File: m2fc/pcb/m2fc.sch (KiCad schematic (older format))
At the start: 70 parts, among them IC101 ADP3335, IC102 STM32F405VGT, IC103 ADP3335, P101 CONN_2, P102 CONN_2, P103 CONN_2, P104 SWD, U101 BAT BOX, U102 ARM SW, U103 HOUSING, U104 HOUSING, U105 HOUSING, U106 MICROSD, U107 MOUNT, U108 MOUNT, U109 MOUNT, U110 MOUNT, U111 MOUNT, U112 MOUNT, X101 8M

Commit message: routing continues
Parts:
- removed GS103: GS2, Connect:GS2, symbol GS2
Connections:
- net GYRO_INT1: now also IC102.44 (PE13); no longer IC102.46 (PE15)
- net HG_ACCEL_INT1: now also IC102.34 (PC5); no longer IC102.33 (PC4)
- net HG_ACCEL_INT2: now also IC102.33 (PC4); no longer IC102.34 (PC5)
- net SJ3: no longer names the net of IC102.62 (PD15)
- no-connect marks 24 -> 25
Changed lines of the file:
@@
 Text Label 4450 3600 0    60   ~ 0
 SD_CD
+Text Label 4450 2300 0    60   ~ 0
+HG_ACCEL_INT1
 Text Label 4450 2200 0    60   ~ 0
-HG_ACCEL_INT1
-Text Label 4450 2300 0    60   ~ 0
 HG_ACCEL_INT2
 Text Label 4450 4300 0    60   ~ 0
@@
 Text Label 8300 3700 0    60   ~ 0
 GYRO_INT1
-Text Label 4450 6700 0    60   ~ 0
+Text Label 4450 6500 0    60   ~ 0
 GYRO_INT1
 Text Label 6600 5950 2    60   ~ 0
@@
 NoConn ~ 4400 4500
 NoConn ~ 4400 4600
-NoConn ~ 4400 6500
 NoConn ~ 3100 6100
 NoConn ~ 3100 6200
@@
 	0    1    1    0
 $EndComp
-$Comp
-L GS2 GS103
-U 1 1 53CB171F
-P 10550 1150
-F 0 "GS103" H 10650 1300 50  0000 C CNN
-F 1 "GS2" H 10650 1001 40  0000 C CNN
-F 2 "Connect:GS2" V 10624 1150 30  0001 C CNN
-F 3 "" H 10550 1150 60  0000 C CNN
-	1    10550 1150
-	0    1    1    0
-$EndComp
 Text Notes 9900 1500 0    60   ~ 0
 CONFIG JUMPERS
@@
 Text Label 10250 900  2    60   ~ 0
 SJ2
-Text Label 10250 1150 2    60   ~ 0
-SJ3
 Text Label 4450 4800 0    60   ~ 0
 SJ1
 Text Label 4450 4900 0    60   ~ 0
 SJ2
-Text Label 4450 5000 0    60   ~ 0
-SJ3
 $Comp
 L STM32F405VGT IC102
@@
 	3100 5300 3050 5300
 Wire Wire Line
-	4400 6700 4450 6700
-Wire Wire Line
 	4400 6600 4450 6600
+Wire Wire Line
+	4400 6500 4450 6500
 Wire Wire Line
 	4400 4400 4450 4400
@@
 	8250 5400 8300 5400
 Wire Wire Line
-	10750 1150 10800 1150
-Wire Wire Line
 	10800 650  10800 1200
 Wire Wire Line
 	10750 900  10800 900
-Connection ~ 10800 1150
 Wire Wire Line
 	10750 650  10800 650
 Connection ~ 10800 900
 Wire Wire Line
-	10350 1150 10250 1150
-Wire Wire Line
 	10350 900  10250 900
 Wire Wire Line
@@
 Wire Wire Line
 	4400 4900 4450 4900
-Wire Wire Line
-	4400 5000 4450 5000
 Wire Wire Line
 	6050 1900 6050 2350
@@
 NoConn ~ 4400 5700
 NoConn ~ 4400 5800
+NoConn ~ 4400 6700
+NoConn ~ 4400 5000
 $EndSCHEMATC

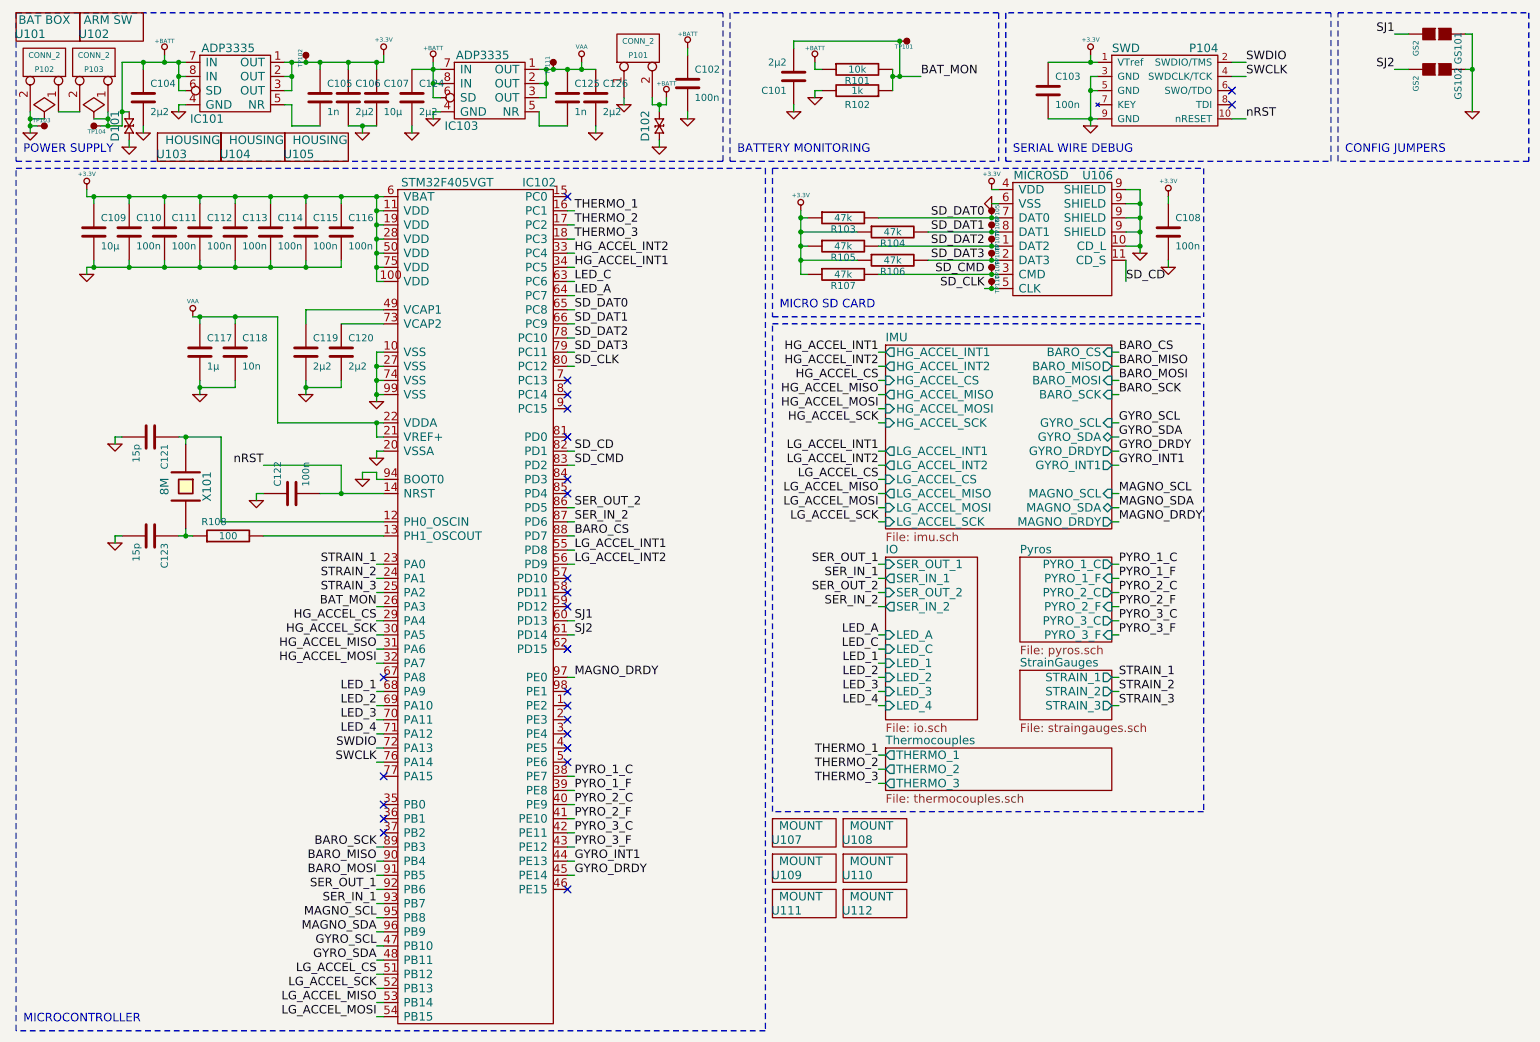
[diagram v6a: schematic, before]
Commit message: routing intensifies
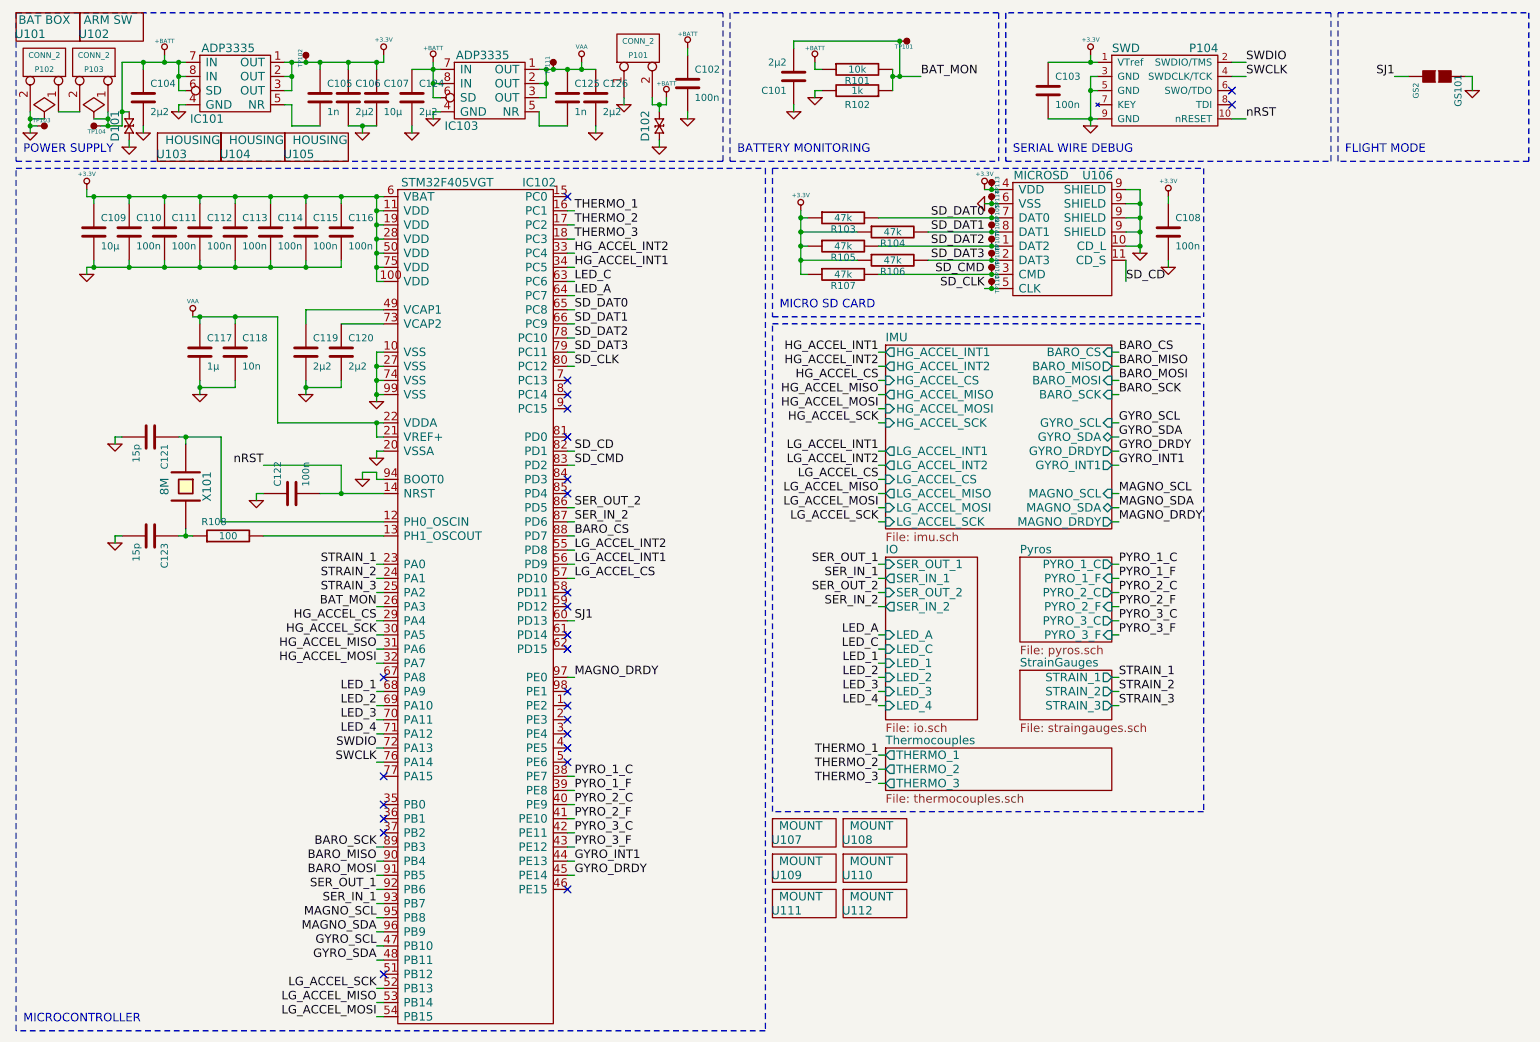
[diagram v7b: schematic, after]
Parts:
- removed GS102: GS2, Connect:GS2, symbol GS2
- added TP113, TP114: TESTPAD, m2fc:TESTPAD, symbol TESTPAD
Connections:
- net +3.3V: now also TP113.1 (TP)
- net GND: now also TP114.1 (TP)
- net LG_ACCEL_CS: now also IC102.57 (PD10); no longer IC102.51 (PB12)
- net LG_ACCEL_INT1: now also IC102.56 (PD9); no longer IC102.55 (PD8)
- net LG_ACCEL_INT2: now also IC102.55 (PD8); no longer IC102.56 (PD9)
- net SJ2: no longer names the net of IC102.61 (PD14)
- no-connect marks 25 -> 26
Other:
- note added: "FLIGHT MODE"
- note removed: "CONFIG JUMPERS"
- moved on the sheet: GS101

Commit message: nc 0
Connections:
- net PYRO_1_F: now also IC102.41 (PE10); no longer IC102.39 (PE8)
- net PYRO_2_C: now also IC102.39 (PE8); no longer IC102.40 (PE9)
- net PYRO_2_F: now also IC102.42 (PE11); no longer IC102.41 (PE10)
- net PYRO_3_C: now also IC102.40 (PE9); no longer IC102.42 (PE11)
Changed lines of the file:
@@
 Text Label 4450 5900 0    60   ~ 0
 PYRO_1_C
-Text Label 4450 6100 0    60   ~ 0
+Text Label 4450 6000 0    60   ~ 0
 PYRO_2_C
-Text Label 4450 6200 0    60   ~ 0
+Text Label 4450 6300 0    60   ~ 0
 PYRO_2_F
 Text Label 8300 3700 0    60   ~ 0
@@
 Text Label 4450 6400 0    60   ~ 0
 PYRO_3_F
-Text Label 4450 6300 0    60   ~ 0
+Text Label 4450 6100 0    60   ~ 0
 PYRO_3_C
-Text Label 4450 6000 0    60   ~ 0
+Text Label 4450 6200 0    60   ~ 0
 PYRO_1_F
 $Comp
